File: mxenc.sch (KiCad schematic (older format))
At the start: 28 parts, among them J4 Conn_01x06, J6 Conn_01x06, J8 Conn_01x06 DNP, SW1 SW_Push, SW2 SW_Push, U1 IMX8MM, U10 24LC16, Y2 Crystal_GND24

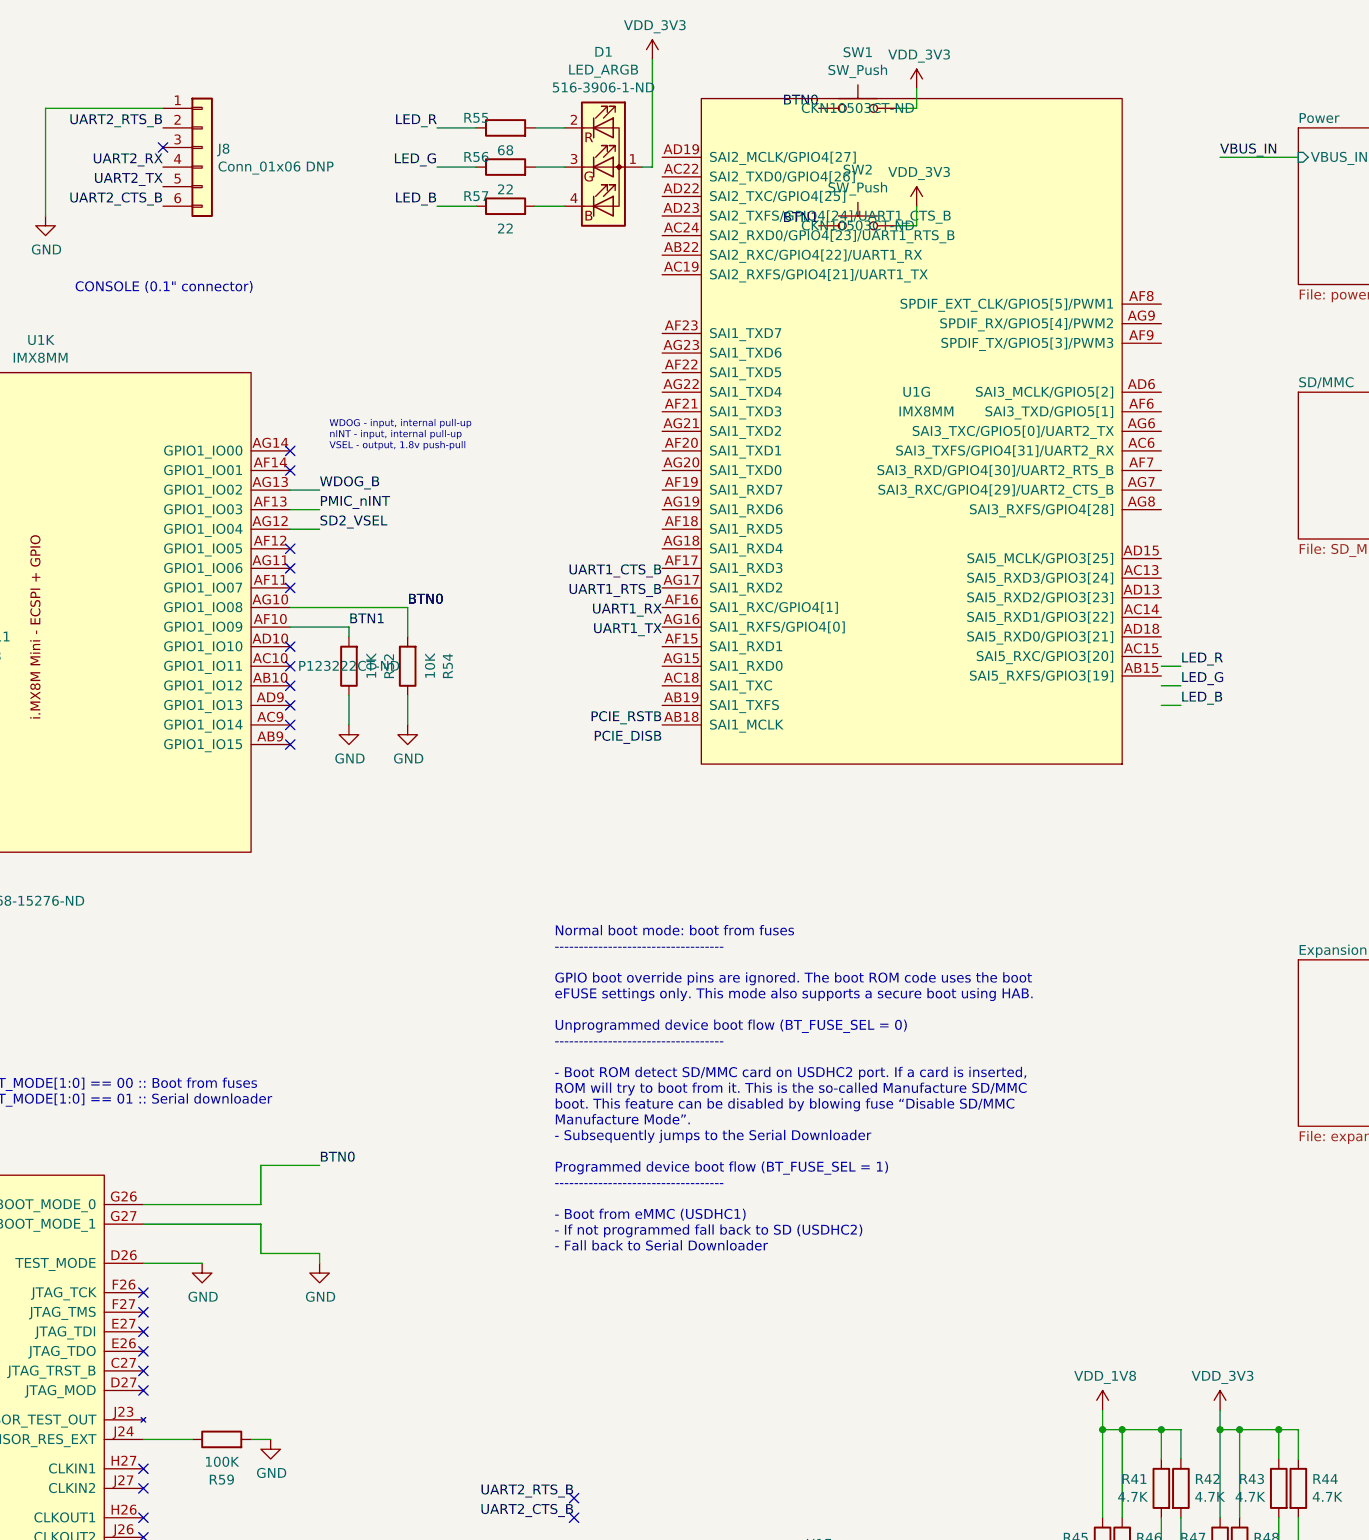
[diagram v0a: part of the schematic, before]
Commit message: More new layout, buttons, and routing
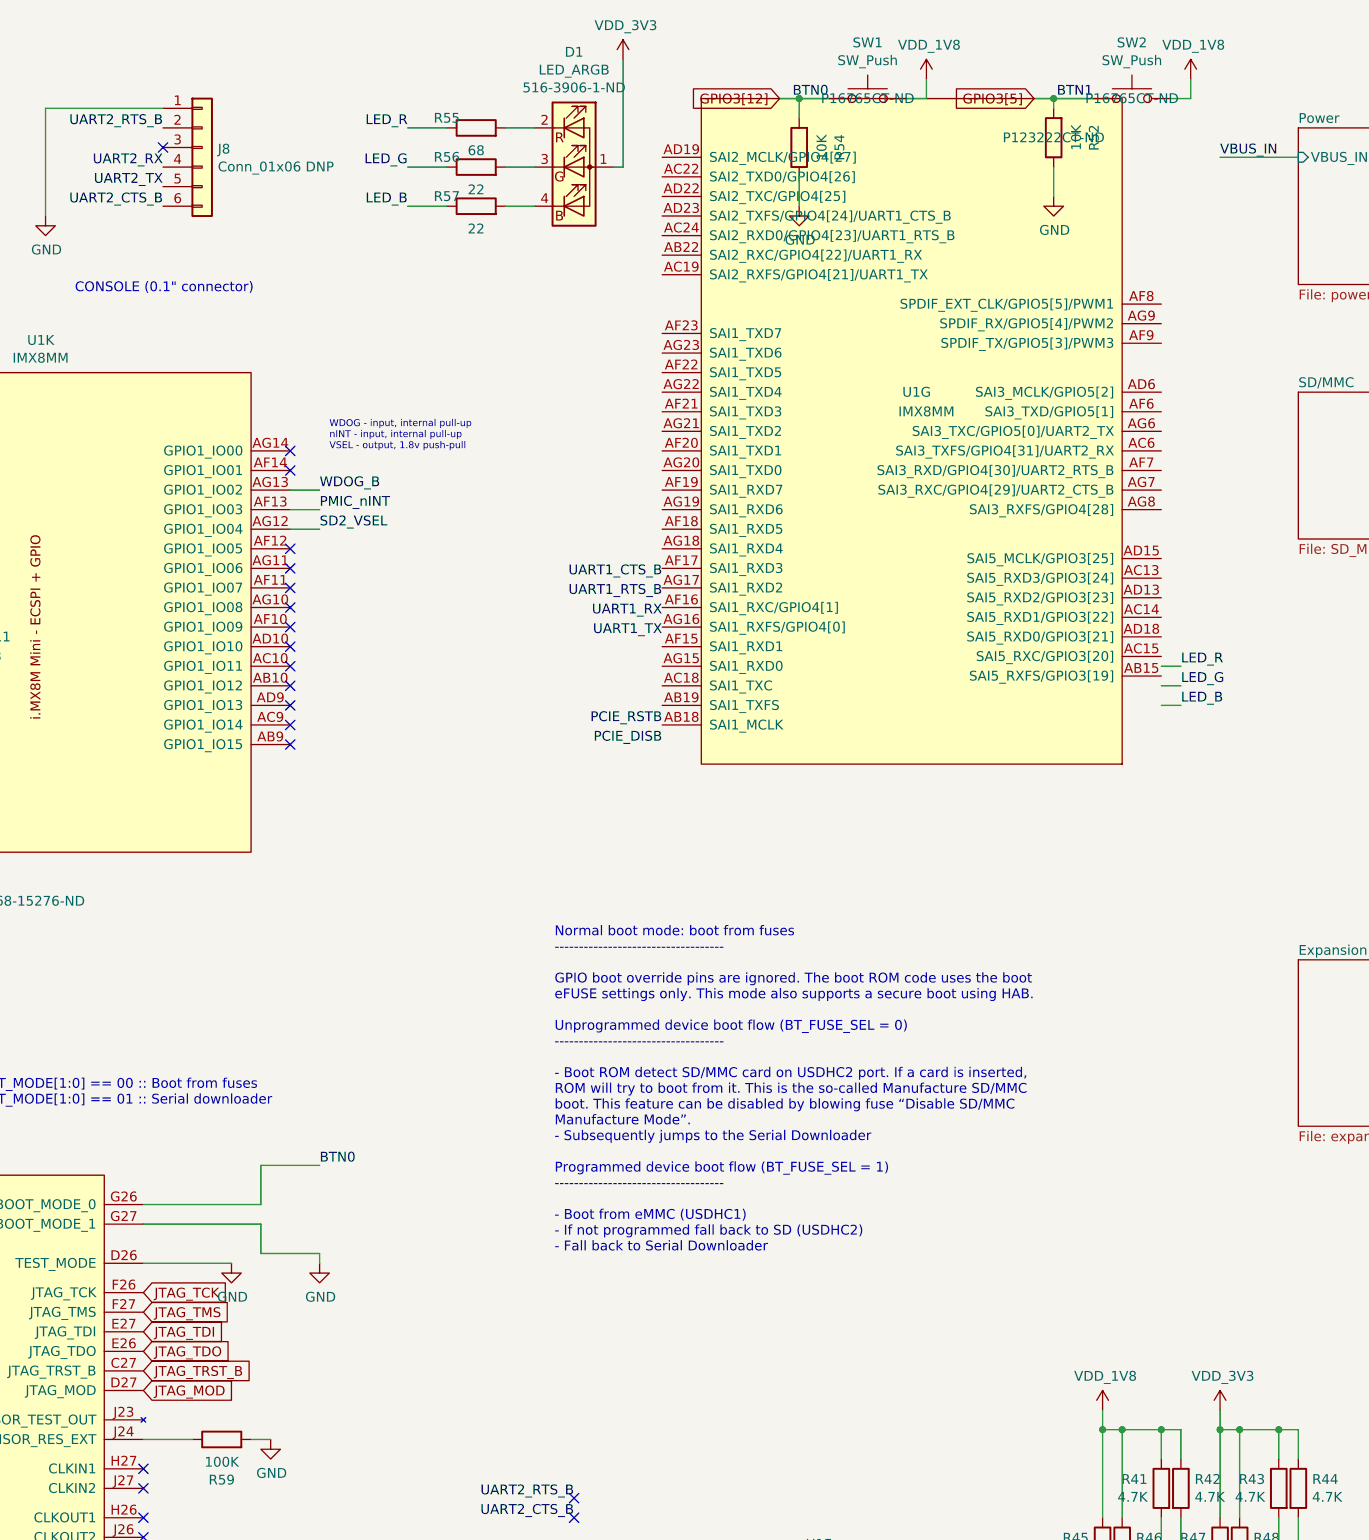
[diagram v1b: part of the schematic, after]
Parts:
- SW1, SW2: footprint Button_Switch_SMD:SW_SPST_PTS810 -> mxenc:SW_SPST_EVQP7C; Mfgr C&K -> Panasonic; Part PTS810 SJK 250 SMTR LFS -> EVQ-P7C01P; Vendorpart CKN10503CT-ND -> P16765CT-ND
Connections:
- net VDD_1V8: now also SW1.2, SW2.2
- net VDD_3V3: no longer SW1.2, SW2.2
- net JTAG_TRST_B: now reaches U1.C27 (JTAG_TRST_B)
- net JTAG_MOD: now reaches U1.D27 (JTAG_MOD)
- net JTAG_TDO: now reaches U1.E26 (JTAG_TDO)
- net JTAG_TDI: now reaches U1.E27 (JTAG_TDI)
- net JTAG_TCK: now reaches U1.F26 (JTAG_TCK)
- net JTAG_TMS: now reaches U1.F27 (JTAG_TMS)
- net BTN0 renamed GPIO3[12]
- net GPIO3[12]: no longer U1.AG10 (GPIO1_IO08)
- net BTN1 renamed GPIO3[5]
- net GPIO3[5]: no longer U1.AF10 (GPIO1_IO09)
- no-connect marks 36 -> 32
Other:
- moved on the sheet: D1, R52, R54, R55, R56, R57, SW1
